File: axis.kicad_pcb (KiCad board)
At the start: 4 copper layers, 66 x 17.5 mm, 46 parts, among them J101 CORTEX-DEBUG, J102 JAE_DX07S016JA3, SW101 SW_Push, SW102 SW_Push, U101 TPS78433QWDRBRQ1, U102 ATSAMD51G, U103 BMM150, U104 BHI160, Y101 32k768

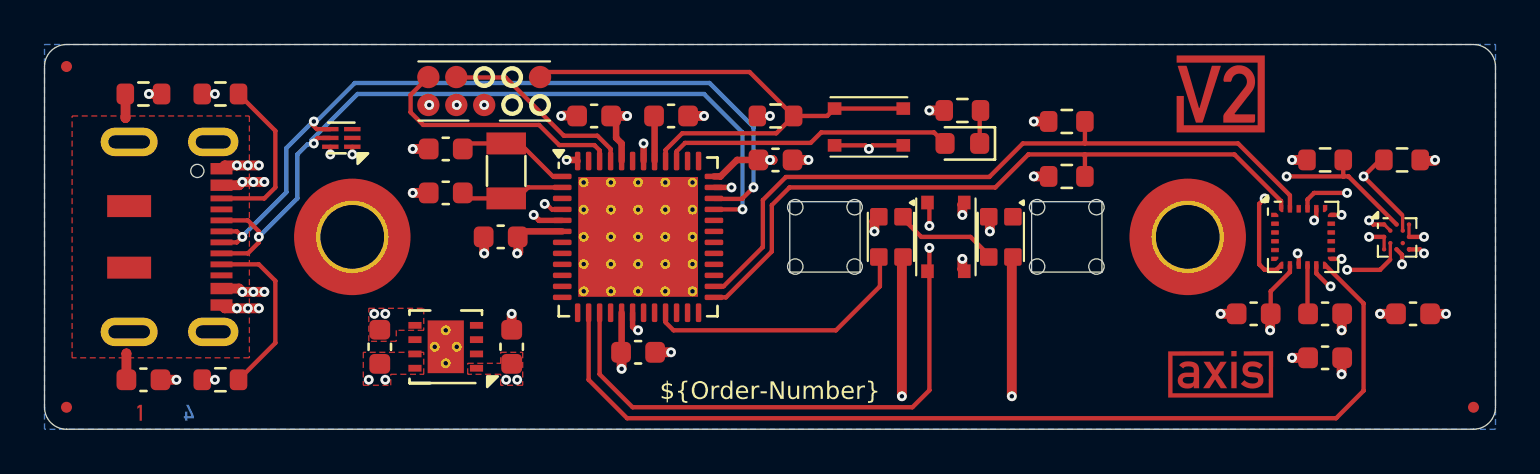
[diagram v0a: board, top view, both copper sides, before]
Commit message: Replace standoffs
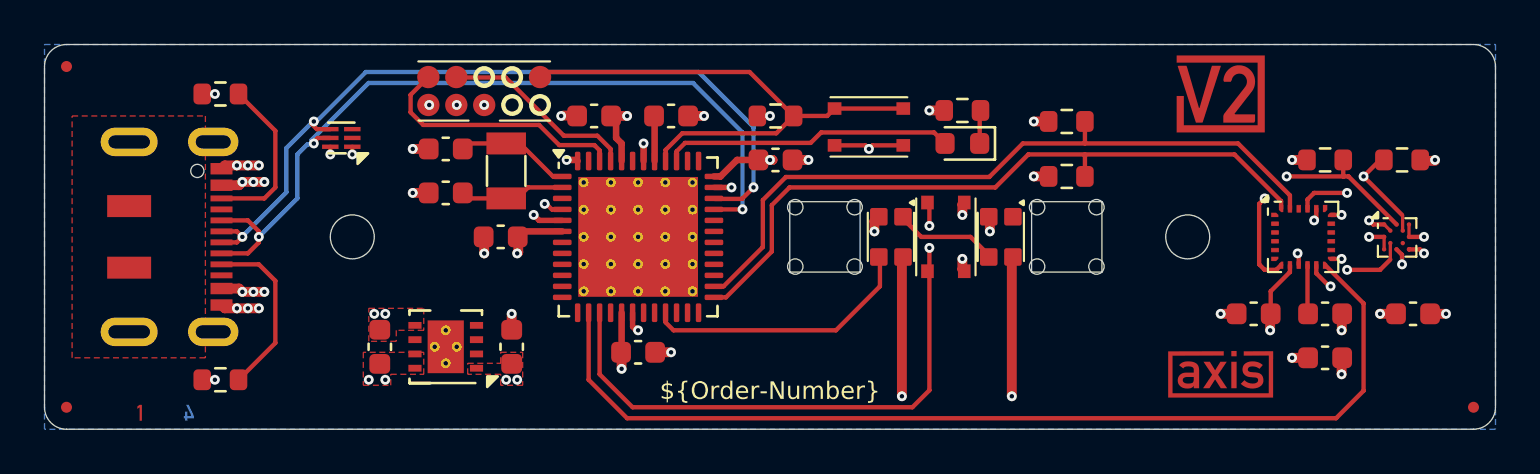
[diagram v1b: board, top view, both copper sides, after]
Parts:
- removed the C110 at (121.5, 112.8)
- removed the R104 at (121.5, 99.8)
- removed SPACER101, SPACER102: 9774030243, V2_Spacer_Wurth:9774030243
- added H101: MountingHole_2mm, V2_Mechanical:MountingHole_2mm, F.Cu at (131.0, 106.2)
- added H102: MountingHole_2mm, V2_Mechanical:MountingHole_2mm, F.Cu at (169.0, 106.2)
- renumbered C111 to C110, C112 to C111, C113 to C112, C114 to C113, R105 to R104, R106 to R105, R107 to R106, R108 to R107, R109 to R108
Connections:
- J102 pad S: Earth -> USB-Shield
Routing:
- net Earth: track 2.30 -> 0.00 mm
- net GND: track 30.8 -> 29.5 mm, vias 44 -> 42
- added copper zone on B.Cu, net GND
- added copper zone on F.Cu, net USB-Shield
- removed copper zone on B.Cu, net Earth
- removed copper zone on F.Cu, net Earth

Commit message: Change capacitors
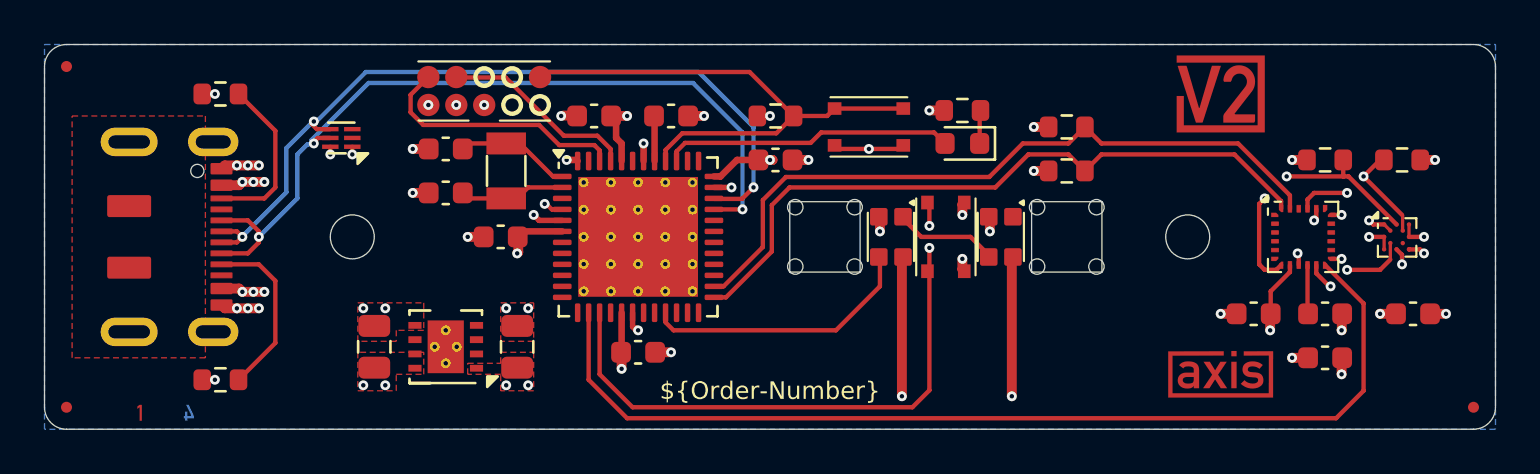
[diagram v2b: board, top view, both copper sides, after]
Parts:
- C106, C107: footprint Capacitor_SMD:C_0603_1608Metric -> Capacitor_SMD:C_0805_2012Metric
- moved C106 0.25 mm to (132.0, 111.2)
- moved C107 0.25 mm to (138.5, 111.2)
- moved R105 0.25 mm to (163.5, 103.2)
- moved R106 0.25 mm to (163.5, 101.2)
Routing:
- net GND: track 29.5 -> 28.7 mm, vias 42 -> 43

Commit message: Update
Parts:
- removed C110: 0u1, Capacitor_SMD:C_0603_1608Metric
- moved C112 7.25 mm to (172.0, 109.8)
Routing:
- net GND: track 28.7 -> 28.0 mm, vias 43 -> 42
- net +3V3: track 22.9 -> 22.2 mm, vias 19 -> 18
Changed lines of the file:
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@@
 		)
 	)
-	(footprint "Capacitor_SMD:C_0603_1608Metric"
-		(layer "F.Cu")
-		(at 172 109.75 180)
-		(descr "Capacitor SMD 0603 (1608 Metric), square (rectangular) end terminal, IPC-7351 nominal, (Body size source: IPC-SM-782 page 76, https://www.pcb-3d.com/wordpress/wp-content/uploads/ipc-sm-782a_amendment_1_and_2.pdf), generated with kicad-footprint-generator")
-		(tags "capacitor")
-		(property "Reference" "C110"
-			(at 0 -1.43 180)
-			(layer "F.SilkS")
-			(hide yes)
-			(effects
-				(font
-					(size 1 1)
-					(thickness 0.15)
-				)
-			)
-		)
-		(property "Value" "0u1"
-			(at 0 1.43 180)
-			(layer "F.Fab")
-			(hide yes)
-			(effects
-				(font
-					(size 1 1)
-					(thickness 0.15)
-				)
-			)
-		)
-		(property "Datasheet" "~"
-			(at 0 0 180)
-			(unlocked yes)
-			(layer "F.Fab")
-			(hide yes)
-			(effects
-				(font
-					(size 1.27 1.27)
-					(thickness 0.15)
-				)
-			)
-		)
-		(property "Description" ""
-			(at 0 0 180)
-			(unlocked yes)
-			(layer "F.Fab")
-			(hide yes)
-			(effects
-				(font
-					(size 1.27 1.27)
-					(thickness 0.15)
-				)
-			)
-		)
-		(property ki_fp_filters "C_*")
-		(sheetname "/")
-		(sheetfile "axis.kicad_sch")
-		(attr smd)
-		(fp_line
-			(start -0.14058 0.51)
-			(end 0.14058 0.51)
-			(stroke
-				(width 0.12)
-				(type solid)
-			)
-			(layer "F.SilkS")
-		)
-		(fp_line
-			(start -0.14058 -0.51)
-			(end 0.14058 -0.51)
-			(stroke
-				(width 0.12)
-				(type solid)
-			)
-			(layer "F.SilkS")
-		)
-		(fp_line
-			(start 1.48 0.73)
-			(end -1.48 0.73)
-			(stroke
-				(width 0.05)
-				(type solid)
-			)
-			(layer "F.CrtYd")
-		)
-		(fp_line
-			(start 1.48 -0.73)
-			(end 1.48 0.73)
-			(stroke
-				(width 0.05)
-				(type solid)
-			)
-			(layer "F.CrtYd")
-		)
-		(fp_line
-			(start -1.48 0.73)
-			(end -1.48 -0.73)
-			(stroke
-				(width 0.05)
-				(type solid)
-			)
-			(layer "F.CrtYd")
-		)
-		(fp_line
-			(start -1.48 -0.73)
-			(end 1.48 -0.73)
-			(stroke
-				(width 0.05)
-				(type solid)
-			)
-			(layer "F.CrtYd")
-		)
-		(fp_line
-			(start 0.8 0.4)
-			(end -0.8 0.4)
-			(stroke
-				(width 0.1)
-				(type solid)
-			)
-			(layer "F.Fab")
-		)
-		(fp_line
-			(start 0.8 -0.4)
-			(end 0.8 0.4)
-			(stroke
-				(width 0.1)
-				(type solid)
-			)
-			(layer "F.Fab")
-		)
-		(fp_line
-			(start -0.8 0.4)
-			(end -0.8 -0.4)
-			(stroke
-				(width 0.1)
-				(type solid)
-			)
-			(layer "F.Fab")
-		)
-		(fp_line
-			(start -0.8 -0.4)
-			(end 0.8 -0.4)
-			(stroke
-				(width 0.1)
-				(type solid)
-			)
-			(layer "F.Fab")
-		)
-		(fp_text user "${REFERENCE}"
-			(at 0 0 180)
-			(layer "F.Fab")
-			(effects
-				(font
-					(size 0.4 0.4)
-					(thickness 0.06)
-				)
-			)
-		)
-		(pad "1" smd roundrect
-			(at -0.775 0 180)
-			(size 0.9 0.95)
-			(layers "F.Cu" "F.Mask" "F.Paste")
-			(roundrect_rratio 0.25)
-			(net 3 "+3V3")
-			(pintype "passive")
-		)
-		(pad "2" smd roundrect
-			(at 0.775 0 180)
-			(size 0.9 0.95)
-			(layers "F.Cu" "F.Mask" "F.Paste")
-			(roundrect_rratio 0.25)
-			(net 1 "GND")
-			(pintype "passive")
-		)
-		(embedded_fonts no)
-		(model "${KICAD9_3DMODEL_DIR}/Capacitor_SMD.3dshapes/C_0603_1608Metric.step"
-			(offset
-				(xyz 0 0 0)
-			)
-			(scale
-				(xyz 1 1 1)
-			)
-			(rotate
-				(xyz 0 0 0)
-			)
-		)
-	)
 	(footprint "V2_LED:WS2812-2020"
 		(layer "F.Cu")
@@
 	(footprint "Capacitor_SMD:C_0603_1608Metric"
 		(layer "F.Cu")
-		(at 179.25 109.75 180)
+		(at 172 109.75 180)
 		(descr "Capacitor SMD 0603 (1608 Metric), square (rectangular) end terminal, IPC-7351 nominal, (Body size source: IPC-SM-782 page 76, https://www.pcb-3d.com/wordpress/wp-content/uploads/ipc-sm-782a_amendment_1_and_2.pdf), generated with kicad-footprint-generator")
 		(tags "capacitor")
@@
 	)
 	(segment
-		(start 177.75 109.738559)
-		(end 177.761441 109.75)
-		(width 0.45)
-		(layer "F.Cu")
-		(net 1)
-	)
-	(segment
 		(start 173.762417 111.762417)
 		(end 173.75 111.75)
@@
 	)
 	(segment
+		(start 171.25 110.5)
+		(end 171.225 110.475)
+		(width 0.45)
+		(layer "F.Cu")
+		(net 1)
+	)
+	(segment
 		(start 143.902102 110.4125)
 		(end 143.902102 110.48758)
@@
 	)
 	(segment
-		(start 170.5 109.75)
-		(end 171.225 109.75)
-		(width 0.45)
-		(layer "F.Cu")
-		(net 1)
-	)
-	(segment
 		(start 125.75 109.5)
 		(end 126.75 109.5)
@@
 	)
 	(segment
+		(start 171.225 110.475)
+		(end 171.225 109.75)
+		(width 0.45)
+		(layer "F.Cu")
+		(net 1)
+	)
+	(segment
 		(start 175.53 105.25)
 		(end 176 105.25)
@@
 	)
 	(segment
-		(start 177.761441 109.75)
-		(end 178.475 109.75)
-		(width 0.45)
-		(layer "F.Cu")
-		(net 1)
-	)
-	(segment
 		(start 151.620986 102.75)
 		(end 151.025 102.75)
@@
 	)
 	(via
-		(at 170.5 109.75)
-		(size 0.45)
-		(drill 0.2)
-		(layers "F.Cu" "B.Cu")
-		(remove_unused_layers yes)
-		(keep_end_layers yes)
-		(free yes)
-		(zone_layer_connections "In1.Cu")
-		(net 1)
-	)
-	(via
 		(at 124.75 99.75)
 		(size 0.45)
@@
 	)
 	(via
-		(at 177.75 109.75)
+		(at 171.25 110.5)
 		(size 0.45)
 		(drill 0.2)
@@
 	)
 	(segment
-		(start 180.699745 109.75)
-		(end 180.025 109.75)
-		(width 0.45)
-		(layer "F.Cu")
-		(net 3)
-	)
-	(segment
 		(start 175.531333 107.251333)
 		(end 175.53 107.25)
@@
 		(net 3)
 	)
-	(segment
-		(start 180.705916 109.743829)
-		(end 180.699745 109.75)
-		(width 0.2)
-		(layer "F.Cu")
-		(net 3)
-	)
 	(via
 		(at 134.46 100.25)
@@
 		(size 0.45)
 		(drill 0.2)
-		(layers "F.Cu" "B.Cu")
-		(remove_unused_layers yes)
-		(keep_end_layers yes)
-		(free yes)
-		(zone_layer_connections "In2.Cu")
-		(net 3)
-	)
-	(via
-		(at 180.75 109.75)
-		(size 0.45)
-		(drill 0.2)

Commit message: Colours
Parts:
- moved C105 0.90 mm to (138.5, 106.8), turned to 90 degrees
- turned C101 to 180 degrees
- renumbered C111 to C110, C112 to C111, C113 to C112
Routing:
- net GND: track 28.0 -> 32.0 mm
- net /VDDCORE: track 2.06 -> 2.76 mm
